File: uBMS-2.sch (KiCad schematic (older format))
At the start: 72 parts, among them Q1 2N7002, Q2 2N7002, Q3 NTD5865NL, U1 LM2576HVS-5, U2 ADS1115IDGS, U3 TLV1117-33, U4 TL431DBV, U5 ESP32-WROOM-32, U6 TSC2012IDT, U7 MCP23017_SS, U8 MCP23008-E_P, U9 VDMG10C0

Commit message: Removed SD card Adapter, added programming port
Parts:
- removed J?: Micro_SD_Card_MEM2061, symbol Connector:Micro_SD_Card_MEM2061
- added C10: 0.1uF, Capacitor_SMD:C_1206_3216Metric, symbol Device:C_Small
- added J1: Conn_01x06, symbol Connector_Generic:Conn_01x06
- R11: value 4.7k -> 10k
- renumbered C10 to C11, C11 to C12, C12 to C13, R28 to R21, R29 to R22, R21 to R23, R22 to R24, R23 to R25, R24 to R26, R25 to R27, R26 to R28, R27 to R29
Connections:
- net labels added: EN, GPIO0
- net labels removed: SD_Detect, SPI_CLK, SPI_CS, SPI_MISO, SPI_MOSI
- wire segments 306 -> 303
- no-connect marks 11 -> 16
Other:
- note added: "CS"
- note added: "MISO"
- note added: "MOSI"
- note added: "Programming Port"
- note added: "SCLK"
- note removed: "MicroSD Card (SPI)"
- note removed: "Should use a card detect version"
- moved on the sheet: BTN3, BTN4, C12, C13, R21, R22, R30, R31

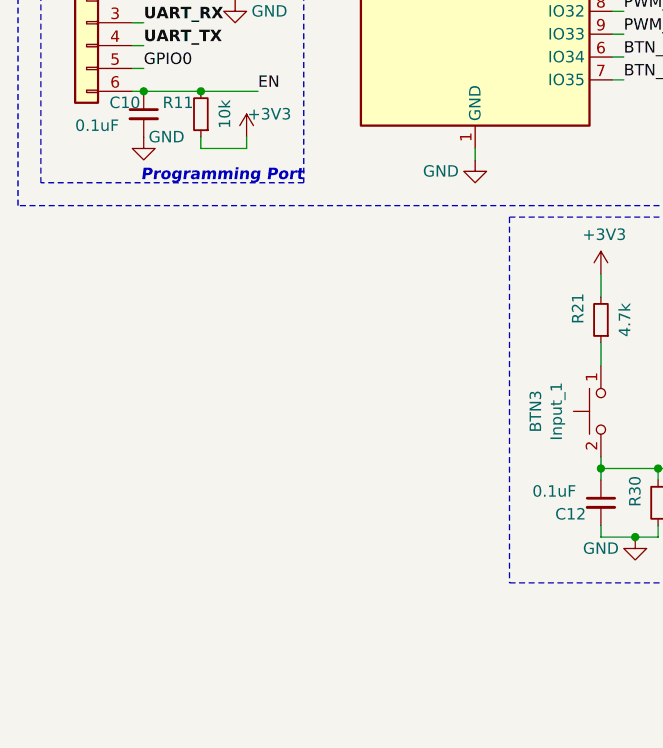
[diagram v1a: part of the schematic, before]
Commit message: Added more power connectors
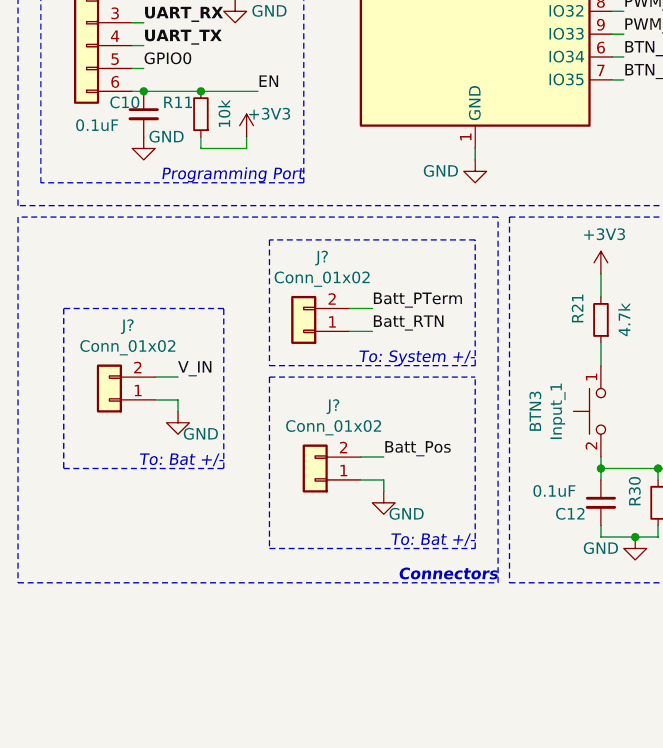
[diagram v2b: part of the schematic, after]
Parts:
- added J? (x3): Conn_01x02, symbol Connector_Generic:Conn_01x02
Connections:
- net Batt_PTerm: now also J?.2 (Pin_2)
- net Batt_Pos: now also J?.2 (Pin_2)
- net Batt_RTN: now also J?.1 (Pin_1)
- net GND: now also J?.1 (Pin_1), J?.1 (Pin_1)
- net V_IN: now also J?.2 (Pin_2)
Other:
- note added: "Connectors"
- note added: "To: Bat +/-"
- note added: "To: System +/-"
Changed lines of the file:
@@
 Wire Notes Line
 	650  2950 1800 2950
-Text Notes 1800 4150 2    50   Italic 10
+Text Notes 1800 4150 2    50   Italic 0
 Programming Port
 $Comp
@@
 Wire Wire Line
 	7300 4150 7300 4200
+$Comp
+L Connector_Generic:Conn_01x02 J?
+U 1 1 5FD4B4ED
+P 950 5100
+F 0 "J?" H 868 4775 50  0000 C CNN
+F 1 "Conn_01x02" H 868 4866 50  0000 C CNN
+F 2 "" H 950 5100 50  0001 C CNN
+F 3 "~" H 950 5100 50  0001 C CNN
+	1    950  5100
+	-1   0    0    1
+$EndComp
+Text Label 1250 5000 0    50   ~ 0
+V_IN
+Wire Wire Line
+	1250 5100 1150 5100
+Wire Wire Line
+	1250 5150 1250 5100
+Wire Wire Line
+	1250 5000 1150 5000
+$Comp
+L Connector_Generic:Conn_01x02 J?
+U 1 1 5FDA1C2F
+P 1800 4800
+F 0 "J?" H 1718 4475 50  0000 C CNN
+F 1 "Conn_01x02" H 1718 4566 50  0000 C CNN
+F 2 "" H 1800 4800 50  0001 C CNN
+F 3 "~" H 1800 4800 50  0001 C CNN
+	1    1800 4800
+	-1   0    0    1
+$EndComp
+Text Label 2100 4700 0    50   ~ 0
+Batt_PTerm
+Wire Wire Line
+	2100 4700 2000 4700
+Text Label 2100 4800 0    50   ~ 0
+Batt_RTN
+Wire Wire Line
+	2100 4800 2000 4800
+$Comp
+L Connector_Generic:Conn_01x02 J?
+U 1 1 5FDF9BBD
+P 1850 5450
+F 0 "J?" H 1768 5125 50  0000 C CNN
+F 1 "Conn_01x02" H 1768 5216 50  0000 C CNN
+F 2 "" H 1850 5450 50  0001 C CNN
+F 3 "~" H 1850 5450 50  0001 C CNN
+	1    1850 5450
+	-1   0    0    1
+$EndComp
+Text Label 2150 5350 0    50   ~ 0
+Batt_Pos
+Wire Wire Line
+	2150 5350 2050 5350
+$Comp
+L power:GND #PWR?
+U 1 1 5FD4C2FF
+P 1250 5150
+F 0 "#PWR?" H 1250 4900 50  0001 C CNN
+F 1 "GND" H 1350 5050 50  0000 C CNN
+F 2 "" H 1250 5150 50  0001 C CNN
+F 3 "" H 1250 5150 50  0001 C CNN
+	1    1250 5150
+	1    0    0    -1
+$EndComp
+$Comp
+L power:GND #PWR?
+U 1 1 5FE34A27
+P 2150 5500
+F 0 "#PWR?" H 2150 5250 50  0001 C CNN
+F 1 "GND" H 2250 5400 50  0000 C CNN
+F 2 "" H 2150 5500 50  0001 C CNN
+F 3 "" H 2150 5500 50  0001 C CNN
+	1    2150 5500
+	1    0    0    -1
+$EndComp
+Wire Wire Line
+	2050 5450 2150 5450
+Wire Wire Line
+	2150 5450 2150 5500
+Wire Notes Line
+	2650 4300 550  4300
+Wire Notes Line
+	550  4300 550  5900
+Wire Notes Line
+	550  5900 2650 5900
+Wire Notes Line
+	2650 5900 2650 4300
+Wire Notes Line
+	750  4700 750  5400
+Wire Notes Line
+	750  5400 1450 5400
+Wire Notes Line
+	1450 5400 1450 4700
+Wire Notes Line
+	1450 4700 750  4700
+Wire Notes Line
+	1650 4400 1650 4950
+Wire Notes Line
+	1650 4950 2550 4950
+Wire Notes Line
+	2550 4950 2550 4400
+Wire Notes Line
+	2550 4400 1650 4400
+Text Notes 2650 5900 2    50   Italic 10
+Connectors
+Text Notes 2550 5750 2    50   Italic 0
+To: Bat +/-
+Text Notes 2550 4950 2    50   Italic 0
+To: System +/-
+Text Notes 1450 5400 2    50   Italic 0
+To: Bat +/-
+Wire Notes Line
+	2550 5750 2550 5000
+Wire Notes Line
+	1650 5000 1650 5750
+Wire Notes Line
+	1650 5000 2550 5000
+Wire Notes Line
+	1650 5750 2550 5750
 $EndSCHEMATC

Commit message: Added ext ADC pin and fixed connection bugs
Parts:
- added J5: Conn_01x01, symbol Connector_Generic:Conn_01x01
- gave numbers to parts that had none: 3
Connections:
- net S0_1 is gone; now on net S0_V: U8.10 (GP0)
- net ADC_Int: now also U5.10 (IO25)
- net ExtADCInput: now also J5.1 (Pin_1)
- no-connect marks 16 -> 15
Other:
- note added: "To: Whatever"
- moved on the sheet: J2
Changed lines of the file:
@@
 	10950 5250 10950 5350
 $Comp
-L power:GND #PWR043
+L power:GND #PWR045
 U 1 1 5F4676CB
 P 10750 5850
-F 0 "#PWR043" H 10750 5600 50  0001 C CNN
+F 0 "#PWR045" H 10750 5600 50  0001 C CNN
 F 1 "GND" H 10900 5800 50  0000 C CNN
 F 2 "" H 10750 5850 50  0001 C CNN
@@
 $EndComp
 $Comp
-L power:GND #PWR042
+L power:GND #PWR044
 U 1 1 5F4F367B
 P 10200 5850
-F 0 "#PWR042" H 10200 5600 50  0001 C CNN
+F 0 "#PWR044" H 10200 5600 50  0001 C CNN
 F 1 "GND" H 10100 5750 50  0000 C CNN
 F 2 "" H 10200 5850 50  0001 C CNN
@@
 $EndComp
 $Comp
-L power:GND #PWR041
+L power:GND #PWR043
 U 1 1 5F6681E3
 P 8500 5850
-F 0 "#PWR041" H 8500 5600 50  0001 C CNN
+F 0 "#PWR043" H 8500 5600 50  0001 C CNN
 F 1 "GND" H 8350 5750 50  0000 C CNN
 F 2 "" H 8500 5850 50  0001 C CNN
@@
 	7550 2900 7550 2800
 $Comp
-L power:GND #PWR045
+L power:GND #PWR047
 U 1 1 5F3615AC
 P 6350 6000
-F 0 "#PWR045" H 6350 5750 50  0001 C CNN
+F 0 "#PWR047" H 6350 5750 50  0001 C CNN
 F 1 "GND" H 6200 5900 50  0000 C CNN
 F 2 "" H 6350 6000 50  0001 C CNN
@@
 	5850 5500 5750 5500
 Text Label 5550 4700 3    50   ~ 0
-S0_1
+S0_V
 Text Label 5650 4700 3    50   ~ 0
 S1_V
@@
 	6350 5750 6350 6000
 $Comp
-L power:GND #PWR044
+L power:GND #PWR046
 U 1 1 5F6C7C43
 P 5000 6000
-F 0 "#PWR044" H 5000 5750 50  0001 C CNN
+F 0 "#PWR046" H 5000 5750 50  0001 C CNN
 F 1 "GND" H 4850 5900 50  0000 C CNN
 F 2 "" H 5000 6000 50  0001 C CNN
@@
 $EndComp
 $Comp
-L power:GND #PWR039
+L power:GND #PWR041
 U 1 1 5F4E72AE
 P 3250 5700
-F 0 "#PWR039" H 3250 5450 50  0001 C CNN
+F 0 "#PWR041" H 3250 5450 50  0001 C CNN
 F 1 "GND" H 3100 5650 50  0000 C CNN
 F 2 "" H 3250 5700 50  0001 C CNN
@@
 $EndComp
 $Comp
-L power:GND #PWR040
+L power:GND #PWR042
 U 1 1 5F5507E9
 P 4250 5700
-F 0 "#PWR040" H 4250 5450 50  0001 C CNN
+F 0 "#PWR042" H 4250 5450 50  0001 C CNN
 F 1 "GND" H 4100 5650 50  0000 C CNN
 F 2 "" H 4250 5700 50  0001 C CNN
@@
 Wire Notes Line
 	4700 4300 4700 5900
-Wire Wire Line
-	5550 4700 5550 4650
 Wire Wire Line
 	5650 4700 5650 4650
@@
 Wire Notes Line
 	650  2950 650  4150
-NoConn ~ 3200 3100
 Wire Wire Line
 	3200 3100 3150 3100
@@
 	7300 4150 7300 4200
 $Comp
-L Connector_Generic:Conn_01x02 J?
+L Connector_Generic:Conn_01x02 J2
 U 1 1 5FD4B4ED
-P 950 5100
-F 0 "J?" H 868 4775 50  0000 C CNN
-F 1 "Conn_01x02" H 868 4866 50  0000 C CNN
-F 2 "" H 950 5100 50  0001 C CNN
-F 3 "~" H 950 5100 50  0001 C CNN
-	1    950  5100
+P 950 4800
+F 0 "J2" H 868 4475 50  0000 C CNN
+F 1 "Conn_01x02" H 868 4566 50  0000 C CNN
+F 2 "" H 950 4800 50  0001 C CNN
+F 3 "~" H 950 4800 50  0001 C CNN
+	1    950  4800
 	-1   0    0    1
 $EndComp
-Text Label 1250 5000 0    50   ~ 0
+Text Label 1250 4700 0    50   ~ 0
 V_IN
 Wire Wire Line
-	1250 5100 1150 5100
-Wire Wire Line
-	1250 5150 1250 5100
-Wire Wire Line
-	1250 5000 1150 5000
-$Comp
-L Connector_Generic:Conn_01x02 J?
+	1250 4800 1150 4800
+Wire Wire Line
+	1250 4850 1250 4800
+Wire Wire Line
+	1250 4700 1150 4700
+$Comp
+L Connector_Generic:Conn_01x02 J3
 U 1 1 5FDA1C2F
 P 1800 4800
-F 0 "J?" H 1718 4475 50  0000 C CNN
+F 0 "J3" H 1718 4475 50  0000 C CNN
 F 1 "Conn_01x02" H 1718 4566 50  0000 C CNN
 F 2 "" H 1800 4800 50  0001 C CNN
@@
 	2100 4800 2000 4800
 $Comp
-L Connector_Generic:Conn_01x02 J?
+L Connector_Generic:Conn_01x02 J4
 U 1 1 5FDF9BBD
 P 1850 5450
-F 0 "J?" H 1768 5125 50  0000 C CNN
+F 0 "J4" H 1768 5125 50  0000 C CNN
 F 1 "Conn_01x02" H 1768 5216 50  0000 C CNN
 F 2 "" H 1850 5450 50  0001 C CNN
@@
 	2150 5350 2050 5350
 $Comp
-L power:GND #PWR?
+L power:GND #PWR039
 U 1 1 5FD4C2FF
-P 1250 5150
-F 0 "#PWR?" H 1250 4900 50  0001 C CNN
-F 1 "GND" H 1350 5050 50  0000 C CNN
-F 2 "" H 1250 5150 50  0001 C CNN
-F 3 "" H 1250 5150 50  0001 C CNN
-	1    1250 5150
-	1    0    0    -1
-$EndComp
-$Comp
-L power:GND #PWR?
+P 1250 4850
+F 0 "#PWR039" H 1250 4600 50  0001 C CNN
+F 1 "GND" H 1350 4750 50  0000 C CNN
+F 2 "" H 1250 4850 50  0001 C CNN
+F 3 "" H 1250 4850 50  0001 C CNN
+	1    1250 4850
+	1    0    0    -1
+$EndComp
+$Comp
+L power:GND #PWR040
 U 1 1 5FE34A27
 P 2150 5500
-F 0 "#PWR?" H 2150 5250 50  0001 C CNN
+F 0 "#PWR040" H 2150 5250 50  0001 C CNN
 F 1 "GND" H 2250 5400 50  0000 C CNN
 F 2 "" H 2150 5500 50  0001 C CNN
@@
 Wire Notes Line
 	2650 5900 2650 4300
-Wire Notes Line
-	750  4700 750  5400
-Wire Notes Line
-	750  5400 1450 5400
-Wire Notes Line
-	1450 5400 1450 4700
-Wire Notes Line
-	1450 4700 750  4700
-Wire Notes Line
-	1650 4400 1650 4950
-Wire Notes Line
-	1650 4950 2550 4950
-Wire Notes Line
-	2550 4950 2550 4400
 Wire Notes Line
 	2550 4400 1650 4400
@@
 Text Notes 2550 5750 2    50   Italic 0
 To: Bat +/-
-Text Notes 2550 4950 2    50   Italic 0
+Text Notes 2550 5000 2    50   Italic 0
 To: System +/-
-Text Notes 1450 5400 2    50   Italic 0
+Text Notes 1600 5100 2    50   Italic 0
 To: Bat +/-
 Wire Notes Line
-	2550 5750 2550 5000
-Wire Notes Line
-	1650 5000 1650 5750
-Wire Notes Line
-	1650 5000 2550 5000
-Wire Notes Line
 	1650 5750 2550 5750
+Text Label 3200 3100 0    50   ~ 0
+ADC_Int
+$Comp
+L Connector_Generic:Conn_01x01 J5
+U 1 1 6009B1C4
+P 800 5500
+F 0 "J5" H 718 5275 50  0000 C CNN
+F 1 "Conn_01x01" H 718 5366 50  0000 C CNN
+F 2 "" H 800 5500 50  0001 C CNN
+F 3 "~" H 800 5500 50  0001 C CNN
+	1    800  5500
+	-1   0    0    1
+$EndComp
+Text Label 1100 5500 0    50   ~ 0
+ExtADCInput
+Wire Wire Line
+	1100 5500 1000 5500
+Wire Notes Line
+	1600 5150 650  5150
+Wire Notes Line
+	1600 5100 1600 4400
+Wire Notes Line
+	650  4400 650  5100
+Wire Notes Line
+	650  5100 1600 5100
+Wire Notes Line
+	650  4400 1600 4400
+Text Notes 1600 5750 2    50   Italic 0
+To: Whatever
+Wire Notes Line
+	1600 5750 650  5750
+Wire Notes Line
+	1600 5150 1600 5750
+Wire Notes Line
+	650  5150 650  5750
+Wire Notes Line
+	1650 5050 2550 5050
+Wire Notes Line
+	2550 5050 2550 5750
+Wire Notes Line
+	2550 5000 1650 5000
+Wire Notes Line
+	1650 4400 1650 5000
+Wire Notes Line
+	2550 4400 2550 5000
+Wire Notes Line
+	1650 5050 1650 5750
+Wire Wire Line
+	5550 4650 5550 4700
 $EndSCHEMATC

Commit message: Added JST power connect and fixed some footprints
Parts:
- removed C10: 0.1uF, Capacitor_SMD:C_1206_3216Metric, symbol Device:C_Small
- removed R11: 10k, Resistor_SMD:R_0603_1608Metric_Pad1.05x0.95mm_HandSolder, symbol Device:R_Small
- J2: footprint (none) -> Connector_JST:JST_PH_S2B-PH-SM4-TB_1x02-1MP_P2.00mm_Horizontal
- R7: footprint (none) -> Resistor_SMD:R_2512_CSNL2512
- renumbered C11 to C10, C12 to C11, C13 to C12, R12 to R11, R13 to R12, R14 to R13, R15 to R14, R16 to R15, R17 to R16, R18 to R17, R19 to R18, R20 to R19, R21 to R20, R22 to R21, R23 to R22, R24 to R23, R25 to R24, R26 to R25, R27 to R26, R28 to R27, R29 to R28, R30 to R29, R31 to R30
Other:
- moved on the sheet: J1

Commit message: Redid programming port for 2x3 config
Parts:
- removed J1: Conn_01x06, symbol Connector_Generic:Conn_01x06
- added J?: Conn_02x03_Counter_Clockwise, Connector_PinHeader_2.54mm:PinHeader_2x03_P2.54mm_Vertical_SMD, symbol Connector_Generic:Conn_02x03_Counter_Clockwise
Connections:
- net +3V3: now also J?.1 (Pin_1)
- net EN: now also J?.6 (Pin_6)
- net GND: now also J?.2 (Pin_2)
- net GPIO0: now also J?.5 (Pin_5)
- net UART_RX: now also J?.3 (Pin_3)
- net UART_TX: now also J?.4 (Pin_4)
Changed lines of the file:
@@
 	1650 1400 1600 1400
-$Comp
-L Connector_Generic:Conn_01x06 J1
-U 1 1 5FA07EE6
-P 900 3650
-F 0 "J1" H 818 4067 50  0000 C CNN
-F 1 "Conn_01x06" H 818 3976 50  0000 C CNN
-F 2 "" H 900 3650 50  0001 C CNN
-F 3 "~" H 900 3650 50  0001 C CNN
-	1    900  3650
-	-1   0    0    -1
-$EndComp
 $Comp
 L power:+3V3 #PWR028
 U 1 1 5FA54DD9
-P 1550 3450
-F 0 "#PWR028" H 1550 3300 50  0001 C CNN
-F 1 "+3V3" H 1565 3623 50  0000 C CNN
-F 2 "" H 1550 3450 50  0001 C CNN
-F 3 "" H 1550 3450 50  0001 C CNN
-	1    1550 3450
-	1    0    0    -1
-$EndComp
-Text Label 1150 3650 0    50   ~ 10
+P 900 3850
+F 0 "#PWR028" H 900 3700 50  0001 C CNN
+F 1 "+3V3" H 915 4023 50  0000 C CNN
+F 2 "" H 900 3850 50  0001 C CNN
+F 3 "" H 900 3850 50  0001 C CNN
+	1    900  3850
+	1    0    0    -1
+$EndComp
+Text Label 1050 4050 2    50   ~ 10
 UART_RX
-Wire Wire Line
-	1150 3650 1100 3650
-Text Label 1150 3750 0    50   ~ 10
+Text Label 1650 4050 0    50   ~ 10
 UART_TX
-Wire Wire Line
-	1150 3750 1100 3750
-Text Label 1150 3850 0    50   ~ 0
+Text Label 1650 3950 0    50   ~ 0
 GPIO0
-Wire Wire Line
-	1150 3850 1100 3850
-Text Label 1150 3950 0    50   ~ 0
+Text Label 1650 3850 0    50   ~ 0
 EN
 $Comp
 L power:GND #PWR029
 U 1 1 5FAD9446
-P 1550 3550
-F 0 "#PWR029" H 1550 3300 50  0001 C CNN
-F 1 "GND" H 1700 3500 50  0000 C CNN
-F 2 "" H 1550 3550 50  0001 C CNN
-F 3 "" H 1550 3550 50  0001 C CNN
-	1    1550 3550
-	1    0    0    -1
-$EndComp
-Wire Wire Line
-	1550 3550 1100 3550
-Wire Wire Line
-	1100 3450 1550 3450
-Wire Notes Line
-	700  3150 1850 3150
-Text Notes 1850 4100 2    50   Italic 0
+P 650 3950
+F 0 "#PWR029" H 650 3700 50  0001 C CNN
+F 1 "GND" H 700 4000 50  0000 C CNN
+F 2 "" H 650 3950 50  0001 C CNN
+F 3 "" H 650 3950 50  0001 C CNN
+	1    650  3950
+	1    0    0    -1
+$EndComp
+Text Notes 2000 4200 2    50   Italic 0
 Programming Port
 Wire Wire Line
@@
 Wire Wire Line
 	5550 4650 5550 4700
-Wire Wire Line
-	1150 3950 1100 3950
-Wire Notes Line
-	700  3150 700  4100
-Wire Notes Line
-	700  4100 1850 4100
-Wire Notes Line
-	1850 4100 1850 3150
+$Comp
+L Connector_Generic:Conn_02x03_Counter_Clockwise J?
+U 1 1 6031BD36
+P 1300 3950
+F 0 "J?" H 1350 4000 50  0000 C CNN
+F 1 "Conn_02x03_Counter_Clockwise" H 1300 4300 50  0000 C CNN
+F 2 "Connector_PinHeader_2.54mm:PinHeader_2x03_P2.54mm_Vertical_SMD" H 1300 3950 50  0001 C CNN
+F 3 "~" H 1300 3950 50  0001 C CNN
+	1    1300 3950
+	1    0    0    -1
+$EndComp
+Wire Wire Line
+	1050 4050 1100 4050
+Wire Wire Line
+	650  3950 1100 3950
+Wire Wire Line
+	900  3850 1100 3850
+Wire Wire Line
+	1650 4050 1600 4050
+Wire Wire Line
+	1650 3950 1600 3950
+Wire Wire Line
+	1650 3850 1600 3850
+Wire Notes Line
+	2000 3550 600  3550
+Wire Notes Line
+	600  3550 600  4200
+Wire Notes Line
+	600  4200 2000 4200
+Wire Notes Line
+	2000 3550 2000 4200
 $EndSCHEMATC

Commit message: Removed additional power connector
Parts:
- removed J2: Conn_01x02, Connector_JST:JST_PH_S2B-PH-SM4-TB_1x02-1MP_P2.00mm_Horizontal, symbol Connector_Generic:Conn_01x02
- J5: footprint (none) -> TestPoint:TestPoint_Pad_D1.5mm
- gave numbers to parts that had none: 1
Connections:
- net V_IN is gone; now on net Batt_Pos: F1.2
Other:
- note added: "Bridge for Power Input"
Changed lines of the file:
@@
 	8750 2000 8750 1950
 $Comp
-L power:GND #PWR030
+L power:GND #PWR028
 U 1 1 5F20A0C9
 P 10650 3550
-F 0 "#PWR030" H 10650 3300 50  0001 C CNN
+F 0 "#PWR028" H 10650 3300 50  0001 C CNN
 F 1 "GND" H 10800 3500 50  0000 C CNN
 F 2 "" H 10650 3550 50  0001 C CNN
@@
 	1650 1400 1600 1400
 $Comp
-L power:+3V3 #PWR028
+L power:+3V3 #PWR029
 U 1 1 5FA54DD9
 P 900 3850
-F 0 "#PWR028" H 900 3700 50  0001 C CNN
+F 0 "#PWR029" H 900 3700 50  0001 C CNN
 F 1 "+3V3" H 915 4023 50  0000 C CNN
 F 2 "" H 900 3850 50  0001 C CNN
@@
 EN
 $Comp
-L power:GND #PWR029
+L power:GND #PWR030
 U 1 1 5FAD9446
 P 650 3950
-F 0 "#PWR029" H 650 3700 50  0001 C CNN
+F 0 "#PWR030" H 650 3700 50  0001 C CNN
 F 1 "GND" H 700 4000 50  0000 C CNN
 F 2 "" H 650 3950 50  0001 C CNN
@@
 Wire Wire Line
 	7300 4150 7300 4200
-$Comp
-L Connector_Generic:Conn_01x02 J2
-U 1 1 5FD4B4ED
-P 950 4800
-F 0 "J2" H 868 4475 50  0000 C CNN
-F 1 "Conn_01x02" H 868 4566 50  0000 C CNN
-F 2 "Connector_JST:JST_PH_S2B-PH-SM4-TB_1x02-1MP_P2.00mm_Horizontal" H 950 4800 50  0001 C CNN
-F 3 "~" H 950 4800 50  0001 C CNN
-	1    950  4800
-	-1   0    0    1
-$EndComp
-Text Label 1250 4700 0    50   ~ 0
+Text Label 1250 4750 0    50   ~ 0
 V_IN
 Wire Wire Line
-	1250 4800 1150 4800
-Wire Wire Line
-	1250 4850 1250 4800
-Wire Wire Line
-	1250 4700 1150 4700
+	1250 4750 1150 4750
 $Comp
 L Connector_Generic:Conn_01x02 J3
@@
 	2150 5350 2050 5350
 $Comp
-L power:GND #PWR037
-U 1 1 5FD4C2FF
-P 1250 4850
-F 0 "#PWR037" H 1250 4600 50  0001 C CNN
-F 1 "GND" H 1350 4750 50  0000 C CNN
-F 2 "" H 1250 4850 50  0001 C CNN
-F 3 "" H 1250 4850 50  0001 C CNN
-	1    1250 4850
-	1    0    0    -1
-$EndComp
-$Comp
 L power:GND #PWR038
 U 1 1 5FE34A27
@@
 To: System +/-
 Text Notes 1600 5100 2    50   Italic 0
-To: Bat +/-
+Bridge for Power Input
 Wire Notes Line
 	1650 5750 2550 5750
@@
 F 0 "J5" H 718 5275 50  0000 C CNN
 F 1 "Conn_01x01" H 718 5366 50  0000 C CNN
-F 2 "" H 800 5500 50  0001 C CNN
+F 2 "TestPoint:TestPoint_Pad_D1.5mm" H 800 5500 50  0001 C CNN
 F 3 "~" H 800 5500 50  0001 C CNN
 	1    800  5500
@@
 	5550 4650 5550 4700
 $Comp
-L Connector_Generic:Conn_02x03_Counter_Clockwise J?
+L Connector_Generic:Conn_02x03_Counter_Clockwise J1
 U 1 1 6031BD36
 P 1300 3950
-F 0 "J?" H 1350 4000 50  0000 C CNN
+F 0 "J1" H 1350 4000 50  0000 C CNN
 F 1 "Conn_02x03_Counter_Clockwise" H 1300 4300 50  0000 C CNN
 F 2 "Connector_PinHeader_2.54mm:PinHeader_2x03_P2.54mm_Vertical_SMD" H 1300 3950 50  0001 C CNN
@@
 Wire Notes Line
 	2000 3550 2000 4200
+Text Label 1150 4750 2    50   ~ 0
+Batt_Pos
 $EndSCHEMATC

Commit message: Refactored some naming
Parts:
- renumbered J3 to J2, J4 to J3, J5 to J4
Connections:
- net Batt_PTerm renamed SYS_Pos
- net Batt_RTN renamed SYS_RTN
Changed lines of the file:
@@
 	5200 2800 5250 2800
 Text Label 5800 3200 0    50   ~ 0
-Batt_RTN
+SYS_RTN
 Wire Wire Line
 	5800 3200 5750 3200
@@
 	10950 5250 10950 5350
 $Comp
-L power:GND #PWR043
+L power:GND #PWR042
 U 1 1 5F4676CB
 P 10750 5850
-F 0 "#PWR043" H 10750 5600 50  0001 C CNN
+F 0 "#PWR042" H 10750 5600 50  0001 C CNN
 F 1 "GND" H 10900 5800 50  0000 C CNN
 F 2 "" H 10750 5850 50  0001 C CNN
@@
 $EndComp
 $Comp
-L power:GND #PWR042
+L power:GND #PWR041
 U 1 1 5F4F367B
 P 10200 5850
-F 0 "#PWR042" H 10200 5600 50  0001 C CNN
+F 0 "#PWR041" H 10200 5600 50  0001 C CNN
 F 1 "GND" H 10100 5750 50  0000 C CNN
 F 2 "" H 10200 5850 50  0001 C CNN
@@
 $EndComp
 $Comp
-L power:GND #PWR041
+L power:GND #PWR040
 U 1 1 5F6681E3
 P 8500 5850
-F 0 "#PWR041" H 8500 5600 50  0001 C CNN
+F 0 "#PWR040" H 8500 5600 50  0001 C CNN
 F 1 "GND" H 8350 5750 50  0000 C CNN
 F 2 "" H 8500 5850 50  0001 C CNN
@@
 Connection ~ 5250 900
 Text Label 7300 2000 0    50   ~ 0
-Batt_PTerm
+SYS_Pos
 Wire Wire Line
 	7300 2000 7250 2000
@@
 	7550 2900 7550 2800
 $Comp
-L power:GND #PWR045
+L power:GND #PWR044
 U 1 1 5F3615AC
 P 6350 6000
-F 0 "#PWR045" H 6350 5750 50  0001 C CNN
+F 0 "#PWR044" H 6350 5750 50  0001 C CNN
 F 1 "GND" H 6200 5900 50  0000 C CNN
 F 2 "" H 6350 6000 50  0001 C CNN
@@
 	6350 5750 6350 6000
 $Comp
-L power:GND #PWR044
+L power:GND #PWR043
 U 1 1 5F6C7C43
 P 5000 6000
-F 0 "#PWR044" H 5000 5750 50  0001 C CNN
+F 0 "#PWR043" H 5000 5750 50  0001 C CNN
 F 1 "GND" H 4850 5900 50  0000 C CNN
 F 2 "" H 5000 6000 50  0001 C CNN
@@
 $EndComp
 $Comp
-L power:GND #PWR039
+L power:GND #PWR038
 U 1 1 5F4E72AE
 P 3250 5700
-F 0 "#PWR039" H 3250 5450 50  0001 C CNN
+F 0 "#PWR038" H 3250 5450 50  0001 C CNN
 F 1 "GND" H 3100 5650 50  0000 C CNN
 F 2 "" H 3250 5700 50  0001 C CNN
@@
 $EndComp
 $Comp
-L power:GND #PWR040
+L power:GND #PWR039
 U 1 1 5F5507E9
 P 4250 5700
-F 0 "#PWR040" H 4250 5450 50  0001 C CNN
+F 0 "#PWR039" H 4250 5450 50  0001 C CNN
 F 1 "GND" H 4100 5650 50  0000 C CNN
 F 2 "" H 4250 5700 50  0001 C CNN
@@
 	1250 4750 1150 4750
 $Comp
-L Connector_Generic:Conn_01x02 J3
+L Connector_Generic:Conn_01x02 J2
 U 1 1 5FDA1C2F
 P 1800 4800
-F 0 "J3" H 1718 4475 50  0000 C CNN
+F 0 "J2" H 1718 4475 50  0000 C CNN
 F 1 "Conn_01x02" H 1718 4566 50  0000 C CNN
 F 2 "" H 1800 4800 50  0001 C CNN
@@
 $EndComp
 Text Label 2100 4700 0    50   ~ 0
-Batt_PTerm
+SYS_Pos
 Wire Wire Line
 	2100 4700 2000 4700
 Text Label 2100 4800 0    50   ~ 0
-Batt_RTN
+SYS_RTN
 Wire Wire Line
 	2100 4800 2000 4800
 $Comp
-L Connector_Generic:Conn_01x02 J4
+L Connector_Generic:Conn_01x02 J3
 U 1 1 5FDF9BBD
 P 1850 5450
-F 0 "J4" H 1768 5125 50  0000 C CNN
+F 0 "J3" H 1768 5125 50  0000 C CNN
 F 1 "Conn_01x02" H 1768 5216 50  0000 C CNN
 F 2 "" H 1850 5450 50  0001 C CNN
@@
 	2150 5350 2050 5350
 $Comp
-L power:GND #PWR038
+L power:GND #PWR037
 U 1 1 5FE34A27
 P 2150 5500
-F 0 "#PWR038" H 2150 5250 50  0001 C CNN
+F 0 "#PWR037" H 2150 5250 50  0001 C CNN
 F 1 "GND" H 2250 5400 50  0000 C CNN
 F 2 "" H 2150 5500 50  0001 C CNN
@@
 ADC_Int
 $Comp
-L Connector_Generic:Conn_01x01 J5
+L Connector_Generic:Conn_01x01 J4
 U 1 1 6009B1C4
 P 800 5500
-F 0 "J5" H 718 5275 50  0000 C CNN
+F 0 "J4" H 718 5275 50  0000 C CNN
 F 1 "Conn_01x01" H 718 5366 50  0000 C CNN
 F 2 "TestPoint:TestPoint_Pad_D1.5mm" H 800 5500 50  0001 C CNN
